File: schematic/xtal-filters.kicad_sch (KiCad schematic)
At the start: 38 parts, among them Y10 9.000, Y11 9.000, Y12 9.000, Y13 9.000, Y14 9.000, Y15 9.000, Y16 9.000, Y17 9.000, Y18 9.000, Y4 9.000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

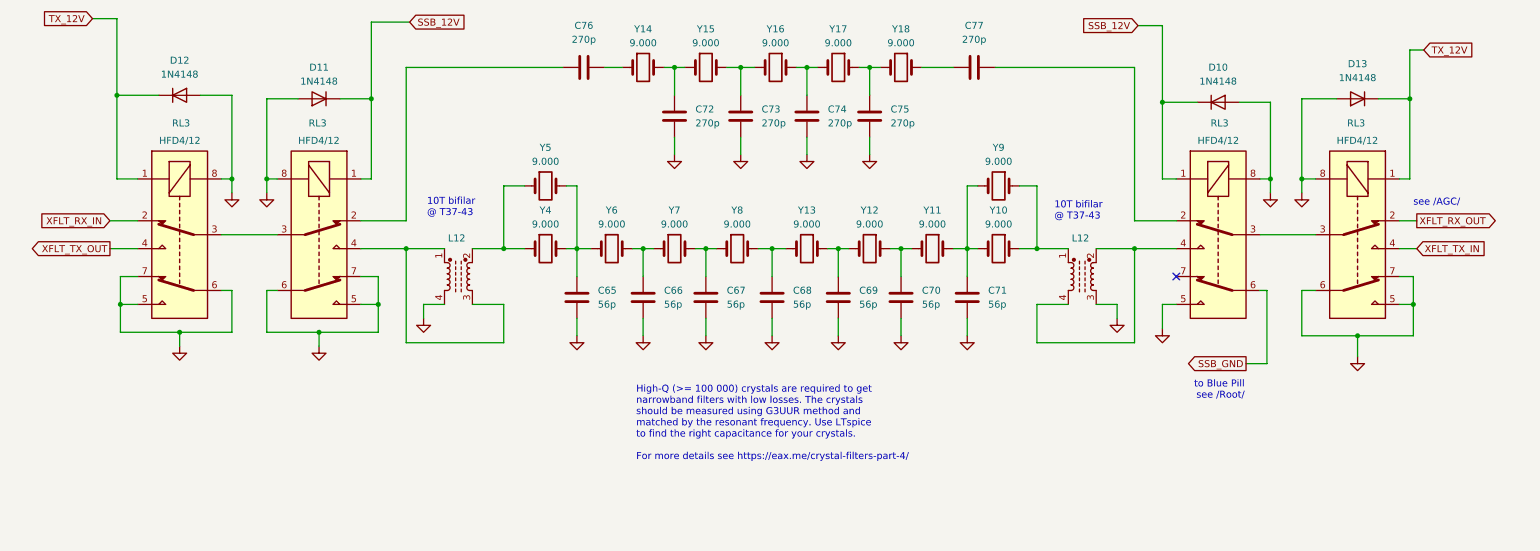
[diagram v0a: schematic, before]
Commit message: Add CW tone generator + other changes
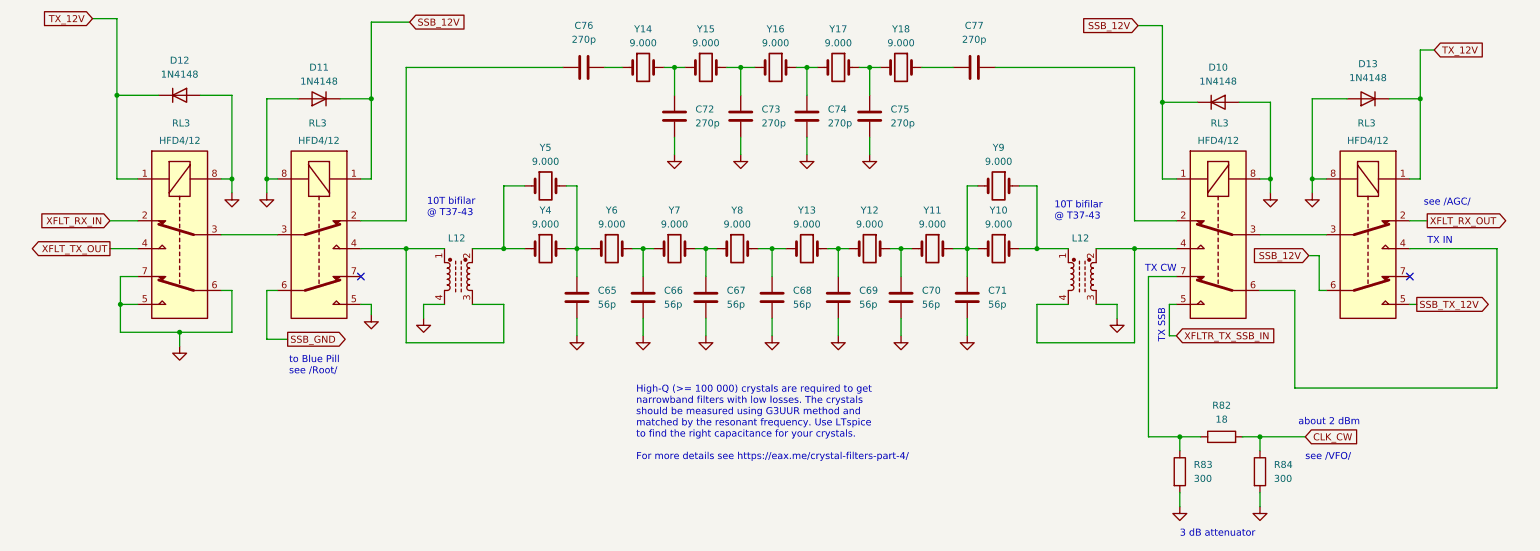
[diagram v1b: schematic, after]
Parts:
- added R82: 18, symbol Device:R
- added R83, R84: 300, symbol Device:R
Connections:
- net GND: now also R83.2, R84.2; no longer RL3.5, RL3.5, RL3.6, RL3.6, RL3.7, RL3.7
- net SSB_12V: now also RL3.6
- net SSB_GND: now also RL3.6; no longer RL3.6
- net at RL3.7: now also R82.1, R83.1
- net XFLT_TX_IN: no longer names the net of RL3.4
- net XFLT_TX_IN: now also RL3.6
- new net CLK_CW: R82.2, R84.1
- new net SSB_TX_12V: RL3.5
- new net XFLTR_TX_SSB_IN: RL3.5
- no-connect marks 1 -> 2
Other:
- note added: "3 dB attenuator"
- note added: "TX CW"
- note added: "TX IN"
- note added: "TX SSB"
- note added: "about 2 dBm"
- note added: "see /VFO/"
- moved on the sheet: D13, RL3

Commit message: Add /TX Common/ schematic sheet
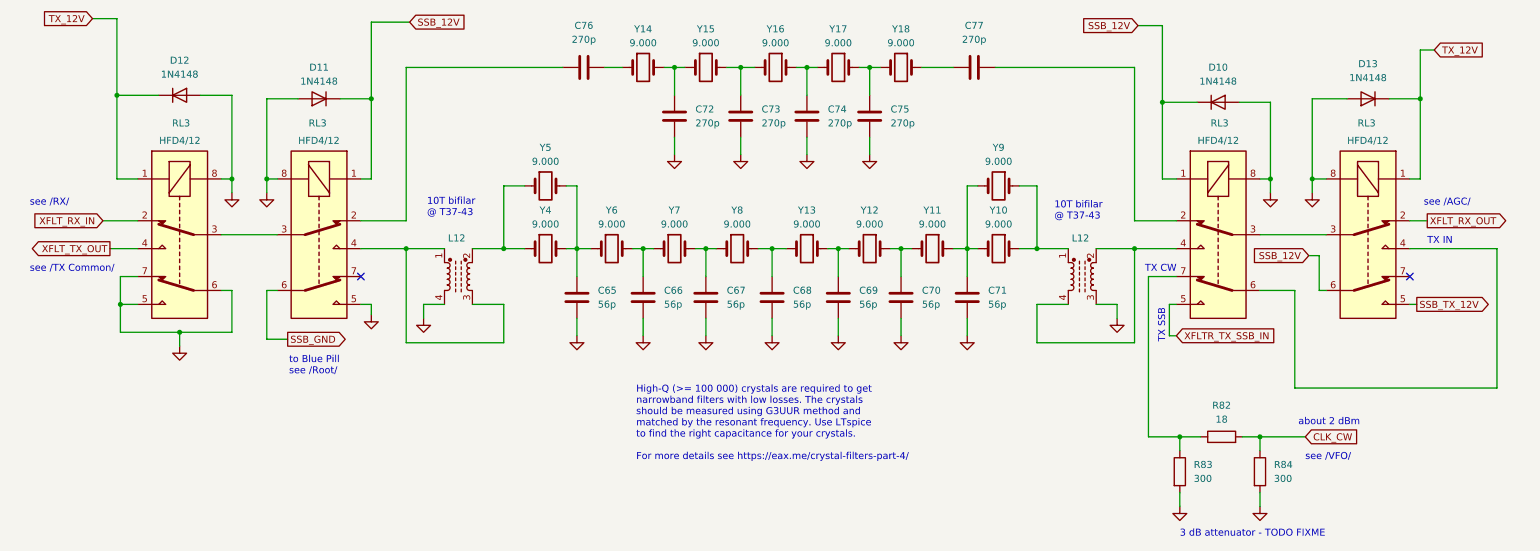
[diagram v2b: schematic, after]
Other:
- note added: "3 dB attenuator - TODO FIXME"
- note added: "see /RX/"
- note added: "see /TX Common/"
- note removed: "3 dB attenuator"
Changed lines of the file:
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@@
     (stroke (width 0) (type default))
   )
-  (wire (pts (xy 29.21 107.315) (xy 34.29 107.315))
+  (wire (pts (xy 27.94 107.315) (xy 34.29 107.315))
     (stroke (width 0) (type default))
   )
@@
     (effects (font (size 1.27 1.27)) (justify left bottom))
   )
-  (text "3 dB attenuator" (at 224.155 165.1 0)
+  (text "3 dB attenuator - TODO FIXME\n" (at 224.155 165.1 0)
     (effects (font (size 1.27 1.27)) (justify left bottom))
   )
@@
     (effects (font (size 1.27 1.27)) (justify left bottom))
   )
+  (text "see /RX/" (at 14.605 104.775 0)
+    (effects (font (size 1.27 1.27)) (justify left bottom))
+  )
   (text "TX IN" (at 269.24 111.76 0)
+    (effects (font (size 1.27 1.27)) (justify left bottom))
+  )
+  (text "see /TX Common/" (at 14.605 116.84 0)
     (effects (font (size 1.27 1.27)) (justify left bottom))
   )
@@
     )
   )
-  (global_label "XFLT_RX_IN" (shape input) (at 29.21 107.315 180) (fields_autoplaced)
+  (global_label "XFLT_RX_IN" (shape input) (at 27.94 107.315 180) (fields_autoplaced)
     (effects (font (size 1.27 1.27)) (justify right))
-    (property "Intersheetrefs" "${INTERSHEET_REFS}" (at 15.6604 107.315 0)
+    (property "Intersheetrefs" "${INTERSHEET_REFS}" (at 14.3904 107.315 0)
       (effects (font (size 1.27 1.27)) (justify right) hide)
     )

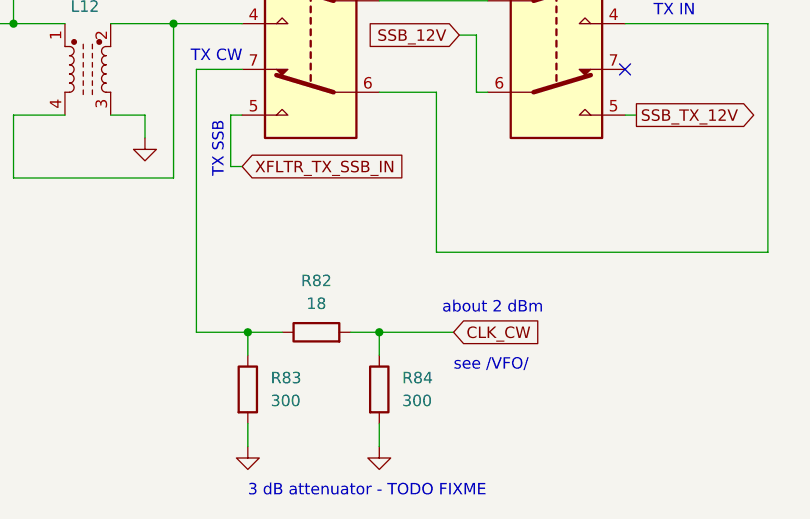
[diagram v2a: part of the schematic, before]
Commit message: Schematic: minor changes
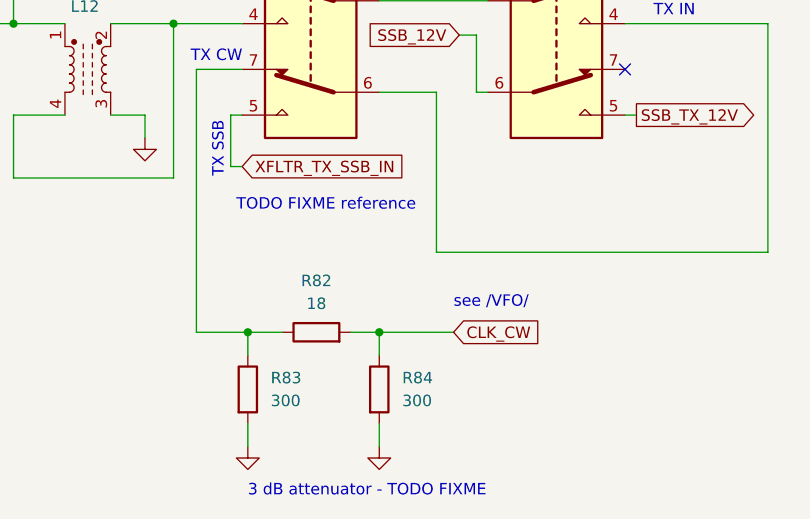
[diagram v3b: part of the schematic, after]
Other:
- note added: "TODO FIXME reference"
- note removed: "about 2 dBm"
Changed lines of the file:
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@@
     (effects (font (size 1.27 1.27)) (justify left bottom))
   )
-  (text "see /VFO/" (at 247.015 151.13 0)
+  (text "see /VFO/" (at 247.015 144.145 0)
+    (effects (font (size 1.27 1.27)) (justify left bottom))
+  )
+  (text "TODO FIXME reference" (at 222.885 133.35 0)
     (effects (font (size 1.27 1.27)) (justify left bottom))
   )
@@
     (effects (font (size 1.27 1.27)) (justify left bottom))
   )
-  (text "about 2 dBm" (at 245.745 144.78 0)
-    (effects (font (size 1.27 1.27)) (justify left bottom))
-  )

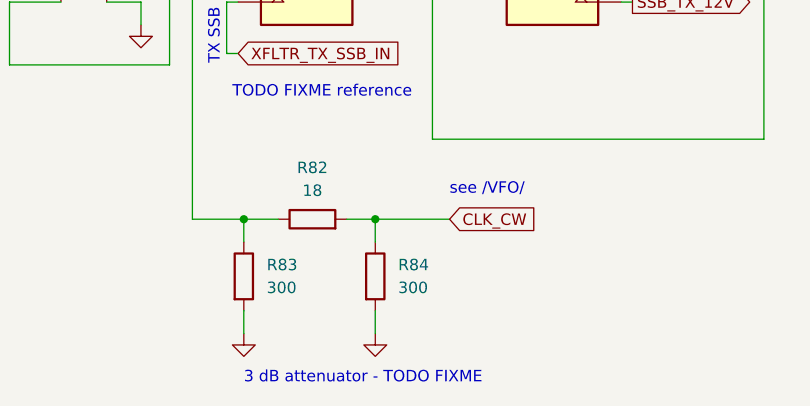
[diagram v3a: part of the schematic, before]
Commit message: Use 4 dB attenuator for CLK_CW instead of 3 dB one + minor changes
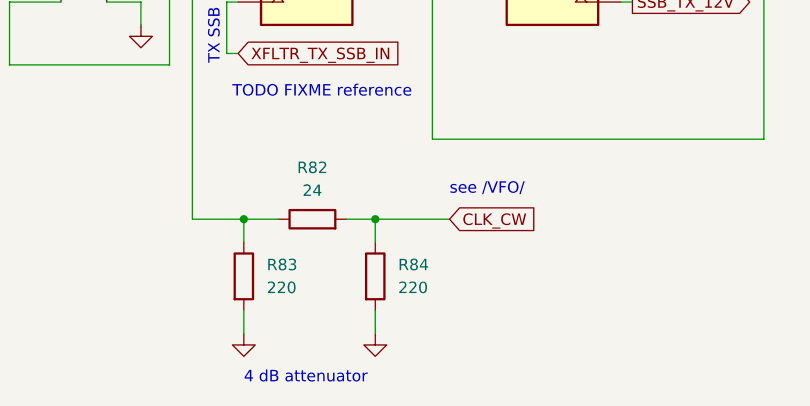
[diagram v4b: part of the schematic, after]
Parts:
- R82: value 18 -> 24
- R83, R84: value 300 -> 220
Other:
- note added: "4 dB attenuator"
- note removed: "3 dB attenuator - TODO FIXME"
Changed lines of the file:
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@@
     (effects (font (size 1.27 1.27)) (justify left bottom))
   )
-  (text "3 dB attenuator - TODO FIXME\n" (at 224.155 165.1 0)
+  (text "4 dB attenuator\n" (at 224.155 165.1 0)
     (effects (font (size 1.27 1.27)) (justify left bottom))
   )
@@
       (effects (font (size 1.27 1.27)) (justify left))
     )
-    (property "Value" "300" (at 226.695 154.305 0)
+    (property "Value" "220" (at 226.695 154.305 0)
       (effects (font (size 1.27 1.27)) (justify left))
     )
@@
       (effects (font (size 1.27 1.27)) (justify left))
     )
-    (property "Value" "300" (at 241.3 154.305 0)
+    (property "Value" "220" (at 241.3 154.305 0)
       (effects (font (size 1.27 1.27)) (justify left))
     )
@@
       (effects (font (size 1.27 1.27)))
     )
-    (property "Value" "18" (at 231.775 143.51 90)
-      (effects (font (size 1.27 1.27)))
-    )
+    (property "Value" "24" (at 231.775 143.51 90)
+      (effects (font (size 1.27 1.27)))
+    )

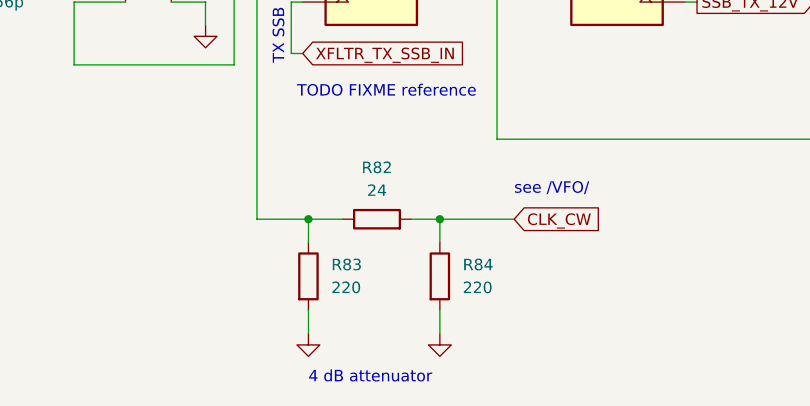
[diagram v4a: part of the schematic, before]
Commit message: Use 6 dB attenuator for CLK_CW
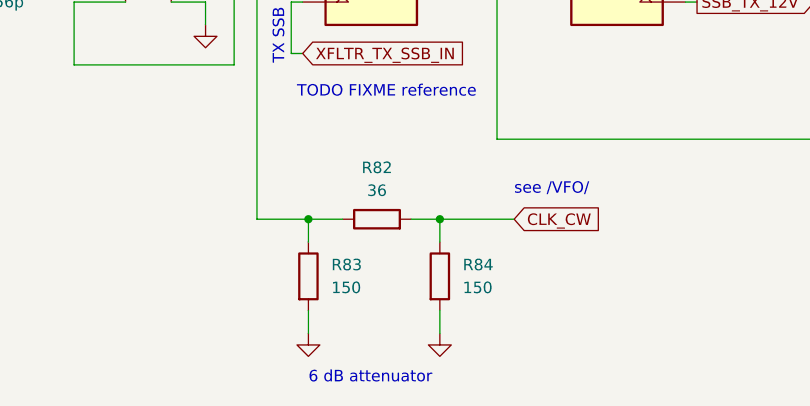
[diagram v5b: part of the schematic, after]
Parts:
- R82: value 24 -> 36
- R83, R84: value 220 -> 150
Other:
- note added: "6 dB attenuator"
- note removed: "4 dB attenuator"
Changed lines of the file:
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@@
     (effects (font (size 1.27 1.27)) (justify left bottom))
   )
-  (text "4 dB attenuator\n" (at 224.155 165.1 0)
+  (text "6 dB attenuator\n" (at 224.155 165.1 0)
     (effects (font (size 1.27 1.27)) (justify left bottom))
   )
@@
       (effects (font (size 1.27 1.27)) (justify left))
     )
-    (property "Value" "220" (at 226.695 154.305 0)
+    (property "Value" "150" (at 226.695 154.305 0)
       (effects (font (size 1.27 1.27)) (justify left))
     )
@@
       (effects (font (size 1.27 1.27)) (justify left))
     )
-    (property "Value" "220" (at 241.3 154.305 0)
+    (property "Value" "150" (at 241.3 154.305 0)
       (effects (font (size 1.27 1.27)) (justify left))
     )
@@
       (effects (font (size 1.27 1.27)))
     )
-    (property "Value" "24" (at 231.775 143.51 90)
-      (effects (font (size 1.27 1.27)))
-    )
+    (property "Value" "36" (at 231.775 143.51 90)
+      (effects (font (size 1.27 1.27)))
+    )

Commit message: Update schematic + minor changes
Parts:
- removed R82: 36, symbol Device:R
- removed R83, R84: 150, symbol Device:R
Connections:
- net XFLTR_TX_SSB_IN is gone; now on net GND: RL3.5
- net GND: now also RL3.6, RL3.7
- net XFLTR_TX_IN: now reaches RL3.4
- net XFLTR_TX_IN: no longer RL3.6
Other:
- note added: "FIXME reference"
- note removed: "6 dB attenuator"
- note removed: "TODO FIXME reference"
- note removed: "TX CW"
- note removed: "TX IN"
- note removed: "TX SSB"
- note removed: "see /VFO/"

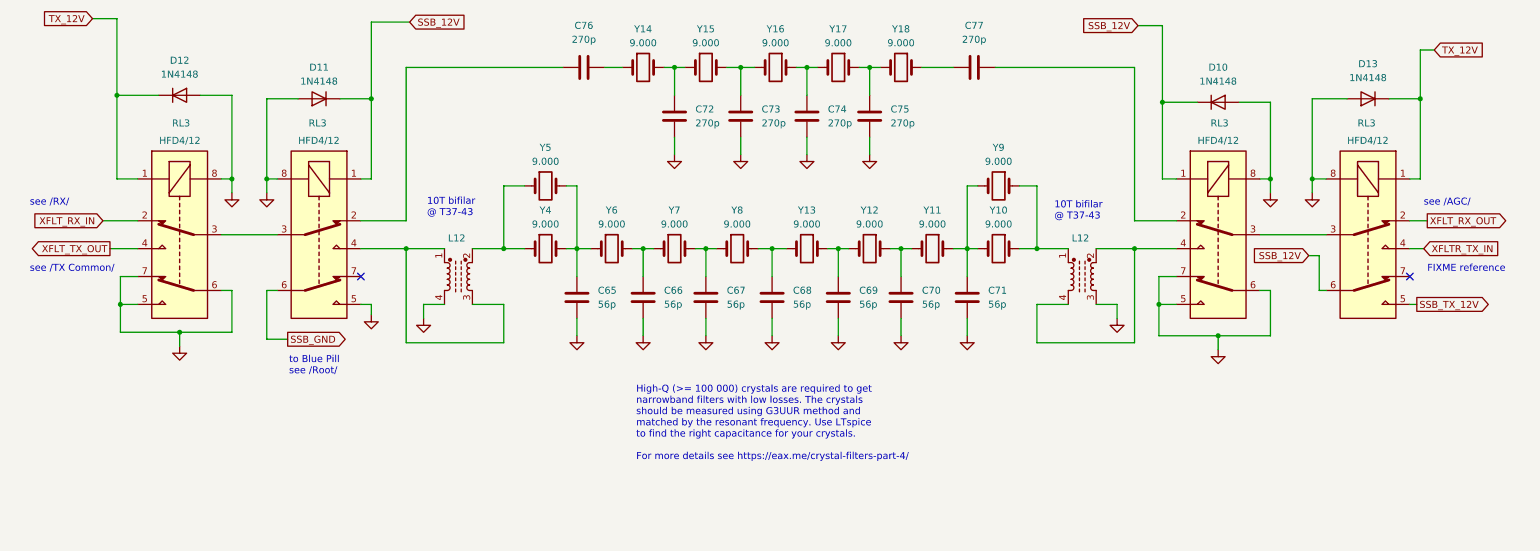
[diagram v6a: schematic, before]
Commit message: Connect relay contact groups in parallel where appropriate
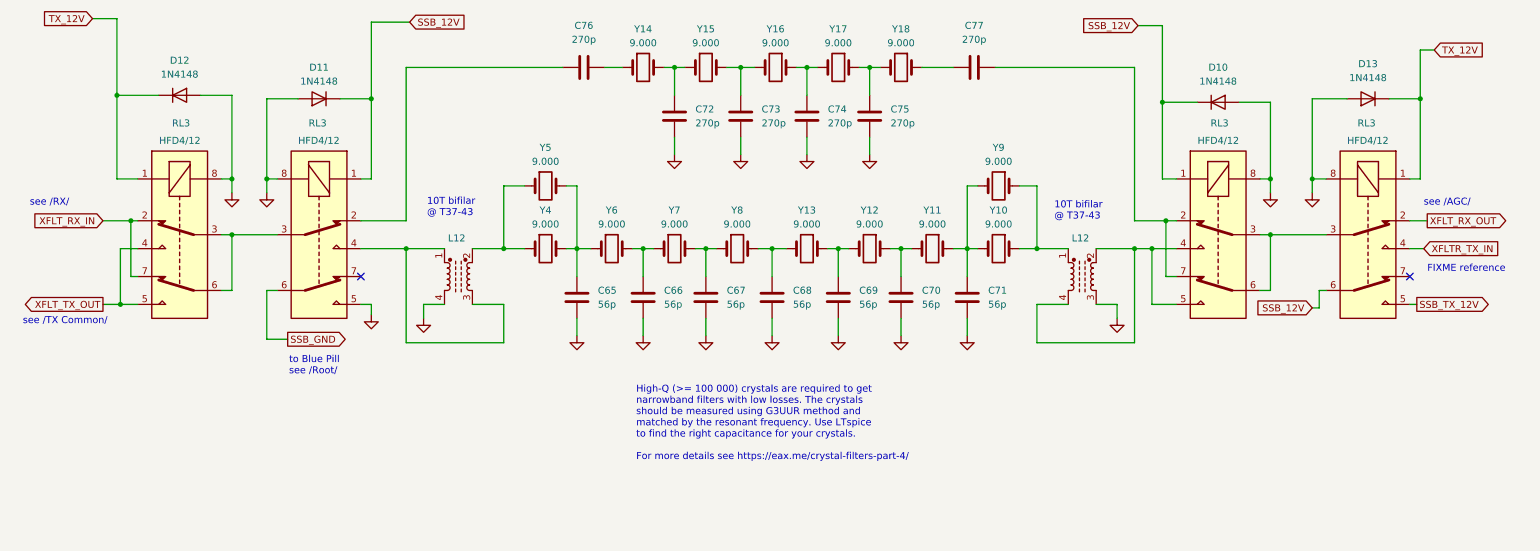
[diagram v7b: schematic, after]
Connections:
- net GND: no longer RL3.5, RL3.5, RL3.6, RL3.6, RL3.7, RL3.7
- net XFLT_RX_IN: now also RL3.7
- net XFLT_TX_OUT: now also RL3.5
- net at RL3.3, RL3.3: now also RL3.6 (x2)
- net at C77.2, RL3.2: now also RL3.7
- net at L12.2, L12.4, RL3.4: now also RL3.5

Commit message: Add PA schematic + some minor changes
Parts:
- L12: value L_Ferrite_Coupled_1423 -> FT37-43
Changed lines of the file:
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@@
       (effects (font (size 1.27 1.27)) (justify left))
     )
-    (property "Value" "L_Ferrite_Coupled_1423" (at 203.2 118.491 90)
+    (property "Value" "FT37-43" (at 203.2 118.491 90)
       (effects (font (size 1.27 1.27)) (justify left) hide)
     )
@@
       (effects (font (size 1.27 1.27)) (justify left))
     )
-    (property "Value" "L_Ferrite_Coupled_1423" (at 89.535 118.491 90)
+    (property "Value" "FT37-43" (at 89.535 118.491 90)
       (effects (font (size 1.27 1.27)) (justify left) hide)
     )
